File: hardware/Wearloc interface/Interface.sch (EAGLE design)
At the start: 33 parts, among them U1 PCA9306DCT, U2 LTC2804-1GN, U3 TXB0104D, U4 MCP1826ADJ

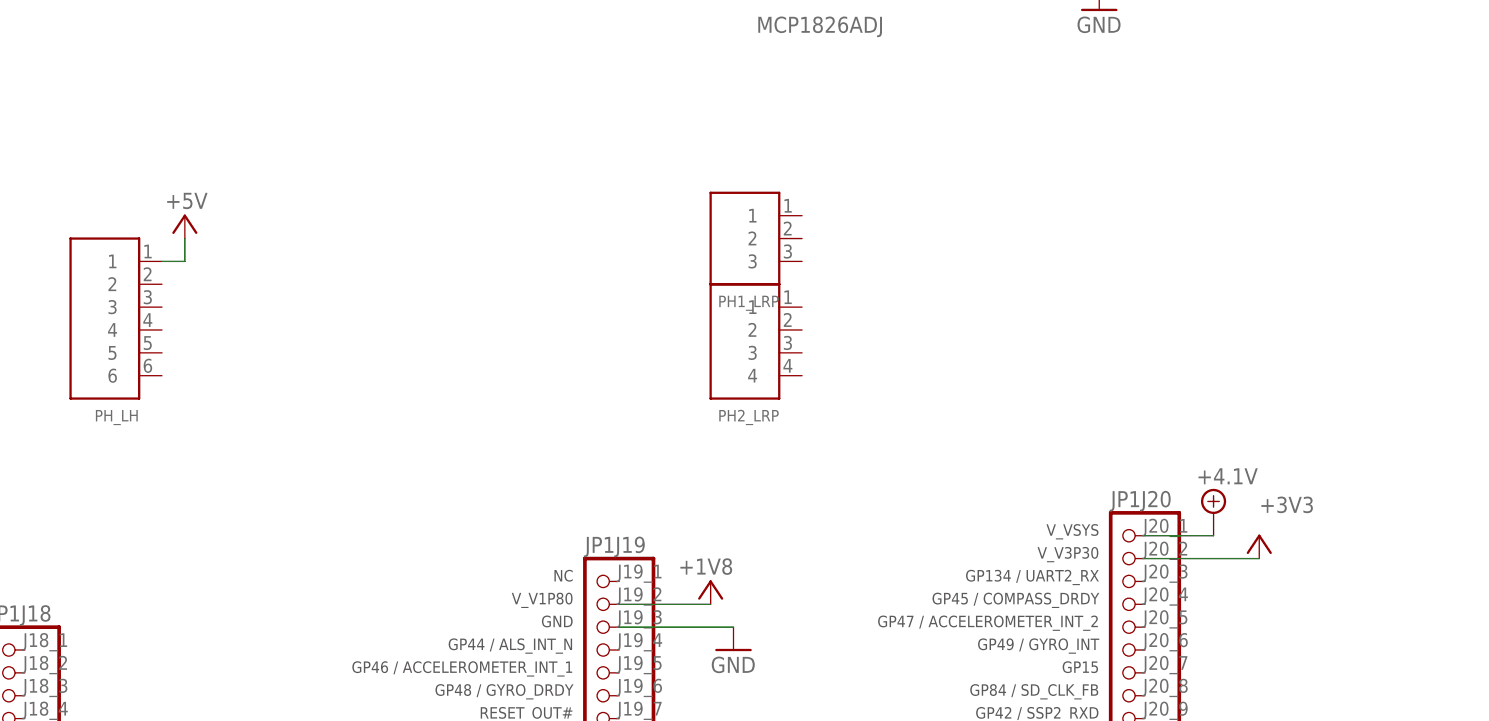
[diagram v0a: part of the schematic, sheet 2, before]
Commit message: worked on interface schematic
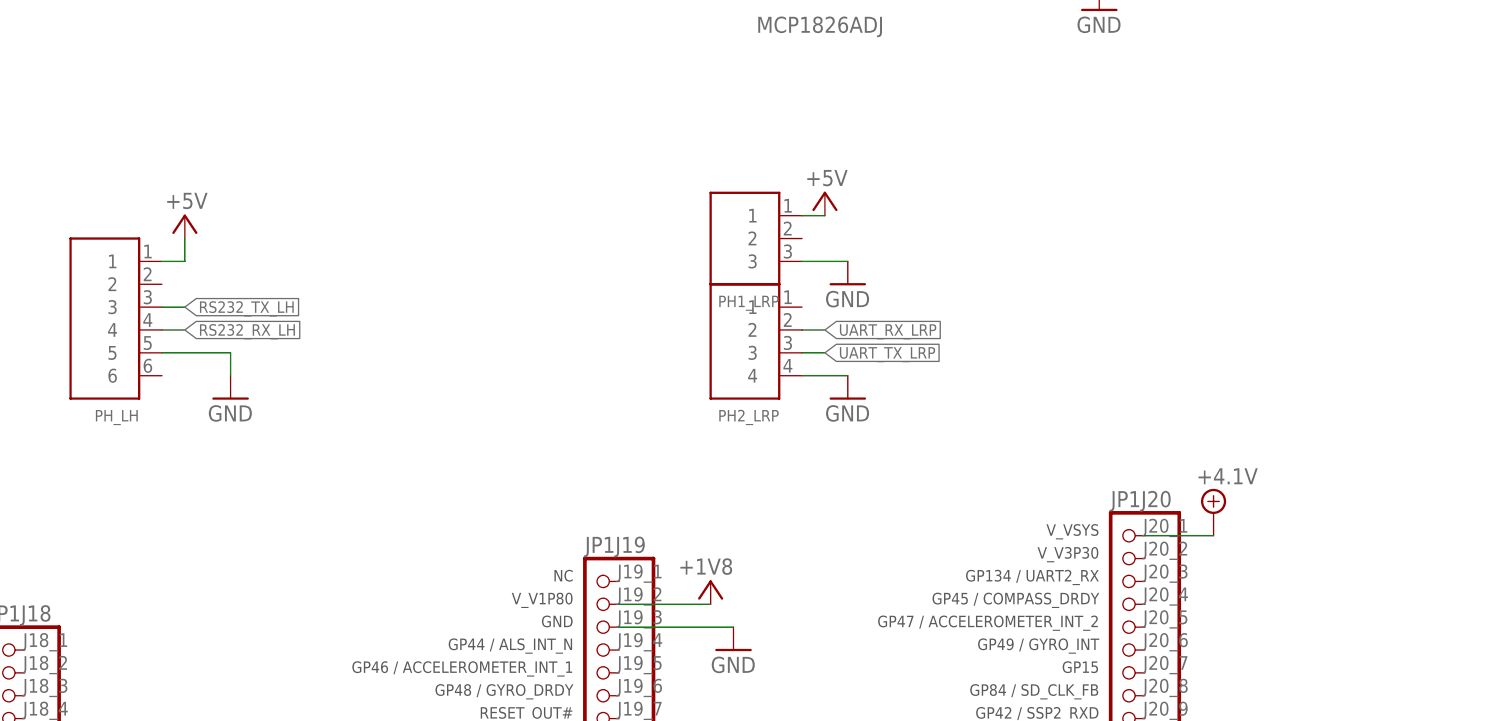
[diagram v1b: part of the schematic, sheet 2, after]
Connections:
- removed net +3V3: C8.1, JP1J20.2, U3.VCCB
- removed net UART_RX_LH: U2.T1OUT
- removed net UART_TX_LH: U2.R1IN
- new net RS232_RX_LH: PH_LH.4, U2.T1OUT
- new net RS232_TX_LH: PH_LH.3, U2.R1IN
- net +5V: now also C8.1, PH1_LRP.1, U3.VCCB
- net GND: now also PH1_LRP.3, PH2_LRP.4, PH_LH.5
- net UART_RX_LRP: now also PH2_LRP.2
- net UART_TX_LRP: now also PH2_LRP.3
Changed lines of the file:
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@@
 <part name="SUPPLY1" library="supply2" deviceset="+4.1V" device=""/>
 <part name="SUPPLY2" library="supply2" deviceset="+4.1V" device=""/>
-<part name="+3V1" library="supply1" deviceset="+3V3" device=""/>
 <part name="+1V1" library="wearloc" deviceset="+1V8" device=""/>
 <part name="GND3" library="supply1" deviceset="GND" device=""/>
@@
 <part name="R11" library="rcl" deviceset="R-EU_" device="R0805"/>
 <part name="+1V4" library="wearloc" deviceset="+1V8" device=""/>
-<part name="+3V3" library="supply1" deviceset="+3V3" device=""/>
 <part name="GND10" library="supply1" deviceset="GND" device=""/>
 <part name="GND11" library="supply1" deviceset="GND" device=""/>
@@
 <part name="P+5" library="supply1" deviceset="+5V" device=""/>
 <part name="P+6" library="supply1" deviceset="+5V" device=""/>
+<part name="P+7" library="supply1" deviceset="+5V" device=""/>
+<part name="GND14" library="supply1" deviceset="GND" device=""/>
+<part name="P+8" library="supply1" deviceset="+5V" device=""/>
+<part name="GND15" library="supply1" deviceset="GND" device=""/>
+<part name="GND16" library="supply1" deviceset="GND" device=""/>
 </parts>
 <sheets>
@@
 <attribute name="VALUE" x="165.1" y="101.6" size="1.778" layer="96" rot="R180"/>
 </instance>
-<instance part="+3V3" gate="G$1" x="215.9" y="99.06" smashed="yes">
-<attribute name="VALUE" x="218.44" y="101.6" size="1.778" layer="96" rot="R180"/>
-</instance>
 <instance part="GND10" gate="1" x="170.18" y="86.36"/>
 <instance part="GND11" gate="1" x="205.74" y="86.36"/>
@@
 <instance part="P+6" gate="1" x="228.6" y="160.02" smashed="yes">
 <attribute name="VALUE" x="231.14" y="162.56" size="1.778" layer="96" rot="R180"/>
+</instance>
+<instance part="P+8" gate="1" x="215.9" y="99.06" smashed="yes">
+<attribute name="VALUE" x="218.44" y="101.6" size="1.778" layer="96" rot="R180"/>
 </instance>
 </instances>
@@
 <junction x="228.6" y="132.08"/>
 <label x="231.14" y="132.08" size="1.016" layer="95" xref="yes"/>
-</segment>
-</net>
-<net name="+3V3" class="0">
-<segment>
-<pinref part="U3" gate="TXB0104" pin="VCCB"/>
-<pinref part="+3V3" gate="G$1" pin="+3V3"/>
-<wire x1="215.9" y1="96.52" x2="205.74" y2="96.52" width="0.1524" layer="91"/>
-<pinref part="C8" gate="G$1" pin="1"/>
-<wire x1="205.74" y1="96.52" x2="193.04" y2="96.52" width="0.1524" layer="91"/>
-<junction x="205.74" y="96.52"/>
 </segment>
 </net>
@@
 <junction x="228.6" y="154.94"/>
 </segment>
+<segment>
+<pinref part="U3" gate="TXB0104" pin="VCCB"/>
+<wire x1="215.9" y1="96.52" x2="205.74" y2="96.52" width="0.1524" layer="91"/>
+<pinref part="C8" gate="G$1" pin="1"/>
+<wire x1="205.74" y1="96.52" x2="193.04" y2="96.52" width="0.1524" layer="91"/>
+<junction x="205.74" y="96.52"/>
+<pinref part="P+8" gate="1" pin="+5V"/>
+</segment>
 </net>
 <net name="N$5" class="0">
@@
 </segment>
 </net>
-<net name="UART_RX_LH" class="0">
+<net name="RS232_RX_LH" class="0">
 <segment>
 <pinref part="U2" gate="LTC2804-1" pin="T1OUT"/>
@@
 </segment>
 </net>
-<net name="UART_TX_LH" class="0">
+<net name="RS232_TX_LH" class="0">
 <segment>
 <pinref part="U2" gate="LTC2804-1" pin="R1IN"/>
@@
 <instance part="SUPPLY1" gate="P" x="203.2" y="149.86"/>
 <instance part="SUPPLY2" gate="P" x="215.9" y="71.12"/>
-<instance part="+3V1" gate="G$1" x="220.98" y="68.58" smashed="yes">
-<attribute name="VALUE" x="220.98" y="71.12" size="1.778" layer="96"/>
-</instance>
 <instance part="+1V1" gate="G$1" x="160.02" y="63.5" smashed="yes">
 <attribute name="VALUE" x="162.56" y="66.04" size="1.778" layer="96" rot="R180"/>
@@
 <attribute name="VALUE" x="53.34" y="88.9" size="1.778" layer="96"/>
 </instance>
+<instance part="P+7" gate="1" x="172.72" y="106.68" smashed="yes">
+<attribute name="VALUE" x="175.26" y="109.22" size="1.778" layer="96" rot="R180"/>
+</instance>
+<instance part="GND14" gate="1" x="106.68" y="83.82"/>
+<instance part="GND15" gate="1" x="175.26" y="96.52"/>
+<instance part="GND16" gate="1" x="175.26" y="83.82"/>
 </instances>
 <busses>
@@
 <pinref part="P+5" gate="1" pin="+5V"/>
 </segment>
+<segment>
+<pinref part="PH1_LRP" gate="JST_XH" pin="1"/>
+<wire x1="170.18" y1="104.14" x2="172.72" y2="104.14" width="0.1524" layer="91"/>
+<pinref part="P+7" gate="1" pin="+5V"/>
+</segment>
 </net>
 <net name="GND" class="0">
@@
 <wire x1="50.8" y1="88.9" x2="50.8" y2="86.36" width="0.1524" layer="91"/>
 <pinref part="GND13" gate="1" pin="GND"/>
+</segment>
+<segment>
+<pinref part="PH_LH" gate="JST_XH" pin="5"/>
+<wire x1="99.06" y1="88.9" x2="106.68" y2="88.9" width="0.1524" layer="91"/>
+<wire x1="106.68" y1="88.9" x2="106.68" y2="86.36" width="0.1524" layer="91"/>
+<pinref part="GND14" gate="1" pin="GND"/>
+</segment>
+<segment>
+<pinref part="PH1_LRP" gate="JST_XH" pin="3"/>
+<pinref part="GND15" gate="1" pin="GND"/>
+<wire x1="170.18" y1="99.06" x2="175.26" y2="99.06" width="0.1524" layer="91"/>
+</segment>
+<segment>
+<pinref part="PH2_LRP" gate="JST_XH" pin="4"/>
+<wire x1="170.18" y1="86.36" x2="175.26" y2="86.36" width="0.1524" layer="91"/>
+<pinref part="GND16" gate="1" pin="GND"/>
 </segment>
 </net>
@@
 </segment>
 </net>
-<net name="+3V3" class="0">
-<segment>
-<pinref part="JP1" gate="J20" pin="2"/>
-<wire x1="208.28" y1="66.04" x2="220.98" y2="66.04" width="0.1524" layer="91"/>
-<pinref part="+3V1" gate="G$1" pin="+3V3"/>
-</segment>
-</net>
 <net name="+1V8" class="0">
 <segment>
@@
 </segment>
 </net>
+<net name="RS232_TX_LH" class="0">
+<segment>
+<pinref part="PH_LH" gate="JST_XH" pin="3"/>
+<wire x1="99.06" y1="93.98" x2="101.6" y2="93.98" width="0.1524" layer="91"/>
+<label x="101.6" y="93.98" size="1.27" layer="95" xref="yes"/>
+</segment>
+</net>
+<net name="RS232_RX_LH" class="0">
+<segment>
+<pinref part="PH_LH" gate="JST_XH" pin="4"/>
+<wire x1="99.06" y1="91.44" x2="101.6" y2="91.44" width="0.1524" layer="91"/>
+<label x="101.6" y="91.44" size="1.27" layer="95" xref="yes"/>
+</segment>
+</net>
+<net name="UART_TX_LRP" class="0">
+<segment>
+<pinref part="PH2_LRP" gate="JST_XH" pin="3"/>
+<wire x1="170.18" y1="88.9" x2="172.72" y2="88.9" width="0.1524" layer="91"/>
+<label x="172.72" y="88.9" size="1.27" layer="95" xref="yes"/>
+</segment>
+</net>
+<net name="UART_RX_LRP" class="0">
+<segment>
+<pinref part="PH2_LRP" gate="JST_XH" pin="2"/>
+<wire x1="170.18" y1="91.44" x2="172.72" y2="91.44" width="0.1524" layer="91"/>
+<label x="172.72" y="91.44" size="1.27" layer="95" xref="yes"/>
+</segment>
+</net>

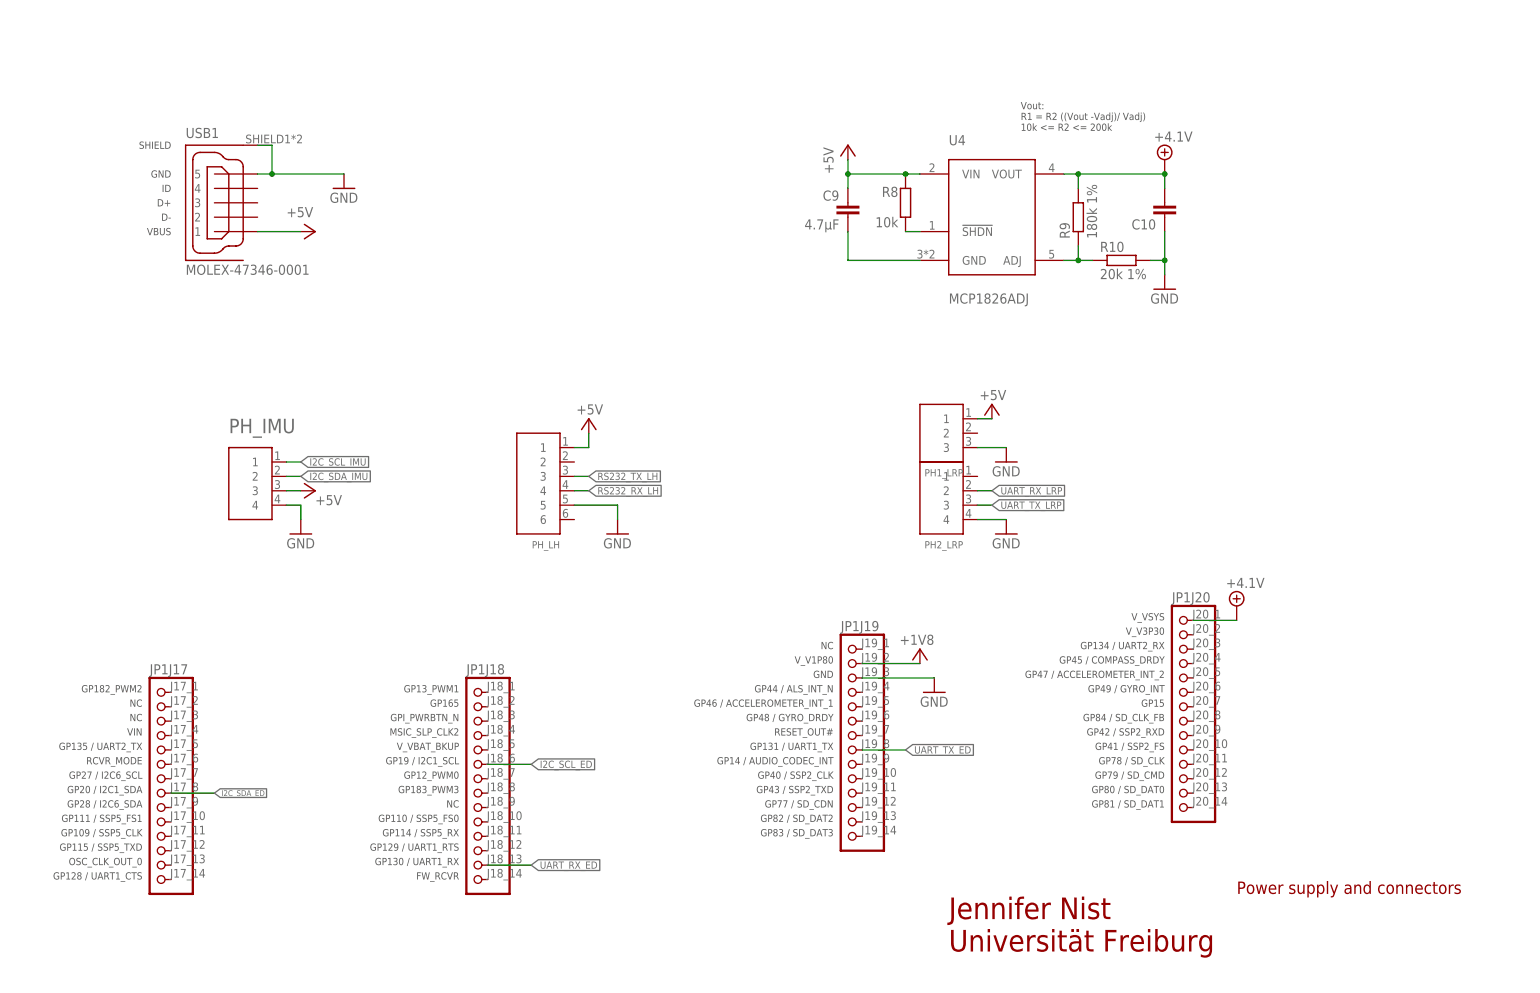
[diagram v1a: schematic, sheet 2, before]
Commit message: worked on interface schematic
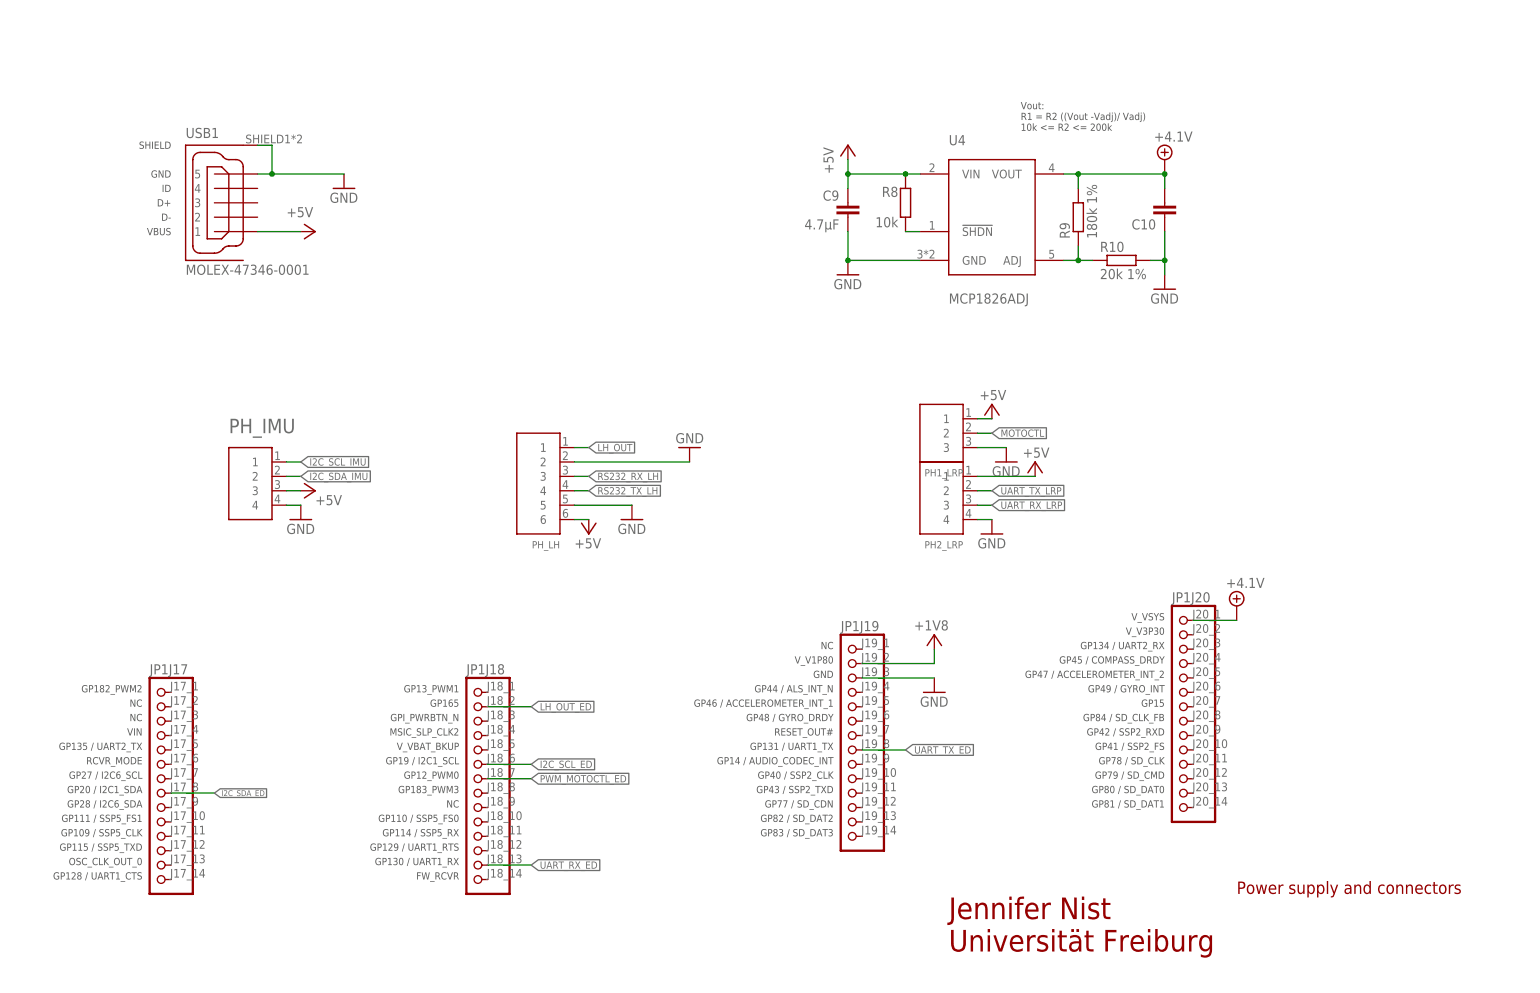
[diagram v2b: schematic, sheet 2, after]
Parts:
- added R12: 1k, rcl:R-EU_R0805
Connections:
- removed net N$1: C9.2, U4.GND
- new net LH_OUT: PH_LH.1, R12.2, U3.B4
- new net LH_OUT_ED: JP1J18.2, U3.A4
- new net MOTOCTL: PH1_LRP.2, U3.B3
- new net PWM_MOTOCTL_ED: JP1J18.7, U3.A3
- net +5V: now also PH2_LRP.1, PH_LH.6, R12.1; no longer PH_LH.1
- net GND: now also C9.2, PH_LH.2, U4.GND
- net RS232_RX_LH: now also PH_LH.3; no longer PH_LH.4
- net RS232_TX_LH: now also PH_LH.4; no longer PH_LH.3
- net UART_RX_LRP: now also PH2_LRP.3; no longer PH2_LRP.2
- net UART_TX_LRP: now also PH2_LRP.2; no longer PH2_LRP.3

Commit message: finished first prototype interface schematic
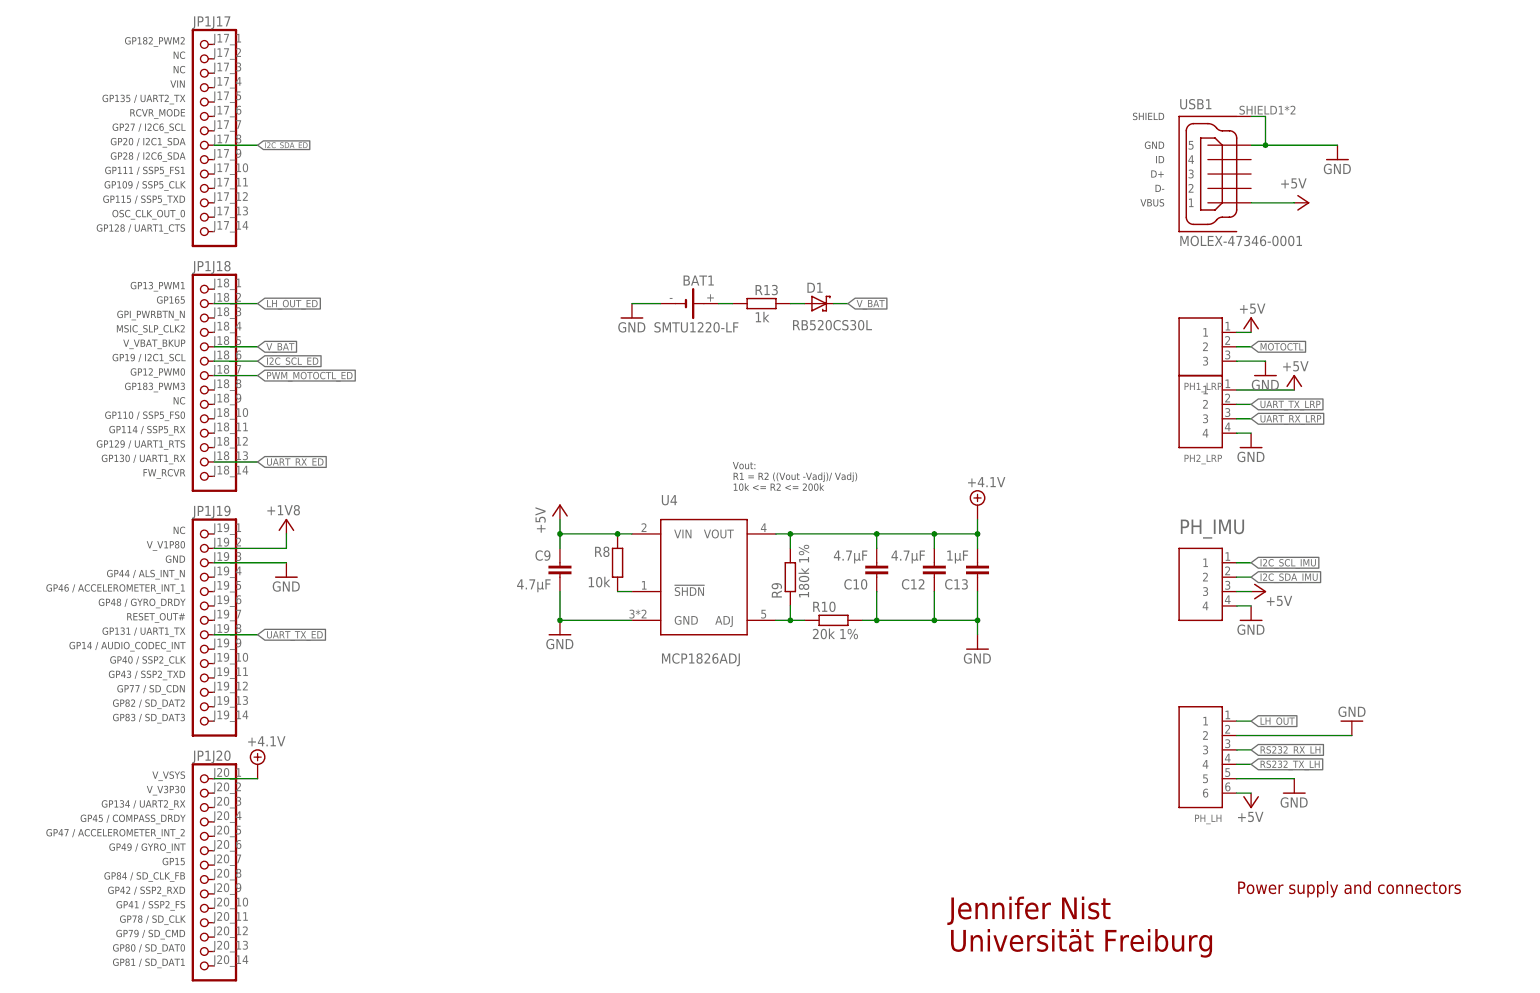
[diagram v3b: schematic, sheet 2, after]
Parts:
- added BAT1: SMTU1220-LF, wearloc:SMTU1220-LF
- added C12: 4.7µF, rcl:C-EUC0805K
- added C13: 1µF, rcl:C-EUC0805K
- added D1: RB520CS30L, wearloc:RB520CS30L
- added R13: 1k, rcl:R-EU_M0805
- added R14: 200, rcl:R-EU_R0805
- added R15: 10k, rcl:R-EU_R0805
- added SW1: SSK-1202, wearloc:SSK-1202
- added TP1, TP2: PTR1B1,27, testpad:PTR1B1,27
- C10: value (none) -> 4.7µF
- C11, C6: value (none) -> 100pF
- JP1: value (none) -> edison
- R1, R11, R7: value (none) -> 10k
- R2, R3: value (none) -> 1k
- R4, R5: value (none) -> 1k5
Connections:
- new net N$1: BAT1.+, R13.1
- new net N$10: R7.2, U2.R2IN
- new net N$11: TP1.TP, U2.T2OUT
- new net N$12: TP2.TP, U2.R2OUT
- new net N$9: D1.A, R13.2
- new net ON/OFF_RS232: R11.2, SW1.1, U2.ON/!OFF
- new net ON/OFF_UART: R15.2, SW1.3, U3.OE
- new net V_BAT: D1.C, JP1J18.5
- net +1V8: now also R14.2
- net +4.1V: now also C12.2, C13.2
- net GND: now also BAT1.-, C12.1, C13.1, R1.2, R11.1, R15.1, R7.1
- net N$3: now also R14.1, SW1.2; no longer R11.2, U2.ON/!OFF
- net N$8: now also R1.1, U2.T2IN; no longer R7.2, U3.OE
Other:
- note added: "Switch to manually select between the two laser sensors."
- moved on the sheet: C1, C10, C11, C2, C3, C4, C5, C6, C7, C8, C9, JP1J17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
